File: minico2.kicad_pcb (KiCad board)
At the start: 2 copper layers, 40 parts, among them J1 USB_C_Receptacle_USB2.0, J2 GDEY0213Z98, Q1 MMBT2222, Q2 MMBT2222, Q3 Q_NMOS_GSD, U1 ESP32-WROOM-32E, U2 CH340C, U3 TLV62568DBV, U4 SHT31-DIS, U5 SCD30

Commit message: Route PCB
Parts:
- removed C3: 6.8pF, Capacitor_SMD:C_0402_1005Metric
- removed C5: 100nF, Capacitor_SMD:C_0402_1005Metric
- removed R7, R8: 10kΩ, Resistor_SMD:R_0402_1005Metric
- removed U4: SHT31-DIS, Sensor_Humidity:Sensirion_DFN-8-1EP_2.5x2.5mm_P0.5mm_EP1.1x1.7mm
- added H1: MountingHole, MountingHole:MountingHole_2.7mm_M2.5, F.Cu at (129.0, 79.0)
- added H2: MountingHole, MountingHole:MountingHole_2.7mm_M2.5, F.Cu at (176.0, 79.0)
- added H3: MountingHole, MountingHole:MountingHole_2.7mm_M2.5, F.Cu at (129.0, 126.0)
- added H4: MountingHole, MountingHole:MountingHole_2.7mm_M2.5, F.Cu at (176.0, 126.0)
- added TP1: TestPoint_Small, TestPoint:TestPoint_Pad_D2.0mm, F.Cu at (130.9, 88.5)
- added TP2: TestPoint_Small, TestPoint:TestPoint_Pad_D2.0mm, F.Cu at (130.9, 91.5)
- added TP3: TestPoint_Small, TestPoint:TestPoint_Pad_D2.0mm, F.Cu at (130.9, 85.4)
- added TP4: TestPoint_Small, TestPoint:TestPoint_Pad_D1.0mm, F.Cu at (139.4, 97.2)
- added TP5: TestPoint_Small, TestPoint:TestPoint_Pad_D1.0mm, F.Cu at (137.0, 94.3)
- added TP6: TestPoint_Small, TestPoint:TestPoint_Pad_D1.0mm, F.Cu at (142.8, 102.5)
- added TP7: TestPoint_Small, TestPoint:TestPoint_Pad_D1.0mm, F.Cu at (138.7, 102.6)
- C1: value 10nF -> 100nF; footprint Capacitor_SMD:C_0402_1005Metric -> Capacitor_SMD:C_0603_1608Metric
- C10, C11, C12, C13, C14, C15, C2, C4, C7, C8: footprint Capacitor_SMD:C_0402_1005Metric -> Capacitor_SMD:C_0603_1608Metric
- C9: value 1µF 25F -> 1µF 25V; footprint Capacitor_SMD:C_0402_1005Metric -> Capacitor_SMD:C_0603_1608Metric
- L2: footprint Inductor_SMD:L_1008_2520Metric -> Inductor_SMD:L_Taiyo-Yuden_NR-60xx
- Q3: value Q_NMOS_GSD -> IRLML0100TRPBF
- R1, R10, R2, R4, R5, R6, R9: footprint Resistor_SMD:R_0402_1005Metric -> Resistor_SMD:R_0603_1608Metric
- R3: value 450kΩ -> 453kΩ; footprint Resistor_SMD:R_0402_1005Metric -> Resistor_SMD:R_0603_1608Metric
- U3: value TLV62568DBV -> AP3418; footprint Package_TO_SOT_SMD:SOT-23-5 -> minico2:SOT-25
- moved J2 146.4 mm to (174.2, 96.2), turned to 90 degrees
- moved R9 144.7 mm to (168.8, 93.7), turned to -90 degrees
- moved D2 144.3 mm to (174.9, 83.2), turned to 180 degrees
- moved D3 135.3 mm to (166.8, 90.6), turned to 90 degrees
- moved R10 131.8 mm to (170.4, 93.7), turned to -90 degrees
- moved C11 127.4 mm to (170.9, 98.0), turned to 180 degrees
- moved R3 120.4 mm to (138.6, 87.2), turned to -90 degrees
- moved L2 120.3 mm to (167.5, 84.9)
- moved R6 113.8 mm to (137.3, 98.8), turned to 90 degrees
- moved R5 113.2 mm to (127.8, 98.8), turned to 90 degrees
- moved U5 109.9 mm to (155.0, 117.0), turned to 90 degrees
- moved C7 103.8 mm to (171.8, 83.9), turned to -90 degrees
- moved C2 99.6 mm to (135.8, 91.0)
- moved C10 96.7 mm to (172.0, 93.7), turned to -90 degrees
- moved U1 95.7 mm to (151.8, 91.0)
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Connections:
- net /SCL renamed /SCD30_SCL
- net /SDA renamed /SCD30_SDA
- net /VCOM renamed Net-(C15-Pad1)
- net Net-(J1-PadA6) renamed /D+
- net Net-(J1-PadA7) renamed /D-
- J2 pad 10: unconnected-(J2-Pad10) -> /~{RES}
- J2 pad 11: unconnected-(J2-Pad11) -> /D/C
- J2 pad 12: unconnected-(J2-Pad12) -> /~{CS}
- J2 pad 13: unconnected-(J2-Pad13) -> /DISPLAY_SCL
- J2 pad 14: unconnected-(J2-Pad14) -> /DISPLAY_SDA
- J2 pad 9: unconnected-(J2-Pad9) -> /BUSY
- U1 pad 26: unconnected-(U1-Pad26) -> /DISPLAY_SDA
- U1 pad 27: unconnected-(U1-Pad27) -> /DISPLAY_SCL
- U1 pad 28: unconnected-(U1-Pad28) -> /~{CS}
- U1 pad 29: unconnected-(U1-Pad29) -> /D/C
- U1 pad 30: unconnected-(U1-Pad30) -> /~{RES}
- U1 pad 31: unconnected-(U1-Pad31) -> /BUSY
- U1 pad 6: /S8_RX -> unconnected-(U1-Pad6)
- U1 pad 7: /S8_TX -> unconnected-(U1-Pad7)
- U2 pad 16: +3V3 -> +5V
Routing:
- net +3V3: track 0.00 -> 123.0 mm, vias 0 -> 4
- net +5V: track 0.00 -> 53.8 mm, vias 0 -> 4
- net /ESP_RX: track 0.00 -> 44.4 mm, vias 0 -> 3
- net /ESP_TX: track 0.00 -> 42.9 mm, vias 0 -> 3
- net /SCD30_SDA: track 0.00 -> 41.0 mm, vias 0 -> 1
- net /SCD30_SCL: track 0.00 -> 36.5 mm
- net /GPIO0: track 0.00 -> 29.5 mm, vias 0 -> 3
- net /D+: track 0.00 -> 28.1 mm
- net /D/C: track 0.00 -> 26.5 mm, vias 0 -> 2
- net /DISPLAY_SCL: track 0.00 -> 26.2 mm, vias 0 -> 2
- net /~{CS}: track 0.00 -> 26.0 mm, vias 0 -> 2
- net /EN: track 0.00 -> 25.9 mm, vias 0 -> 3
- net /D-: track 0.00 -> 25.9 mm
- net /DISPLAY_SDA: track 0.00 -> 25.5 mm, vias 0 -> 2
- net GND: track 0.00 -> 24.9 mm, vias 0 -> 27
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- added copper zone on B.Cu, net GND
- added copper zone on F.Cu, net GND
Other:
- board outline added: 55 x 55 mm

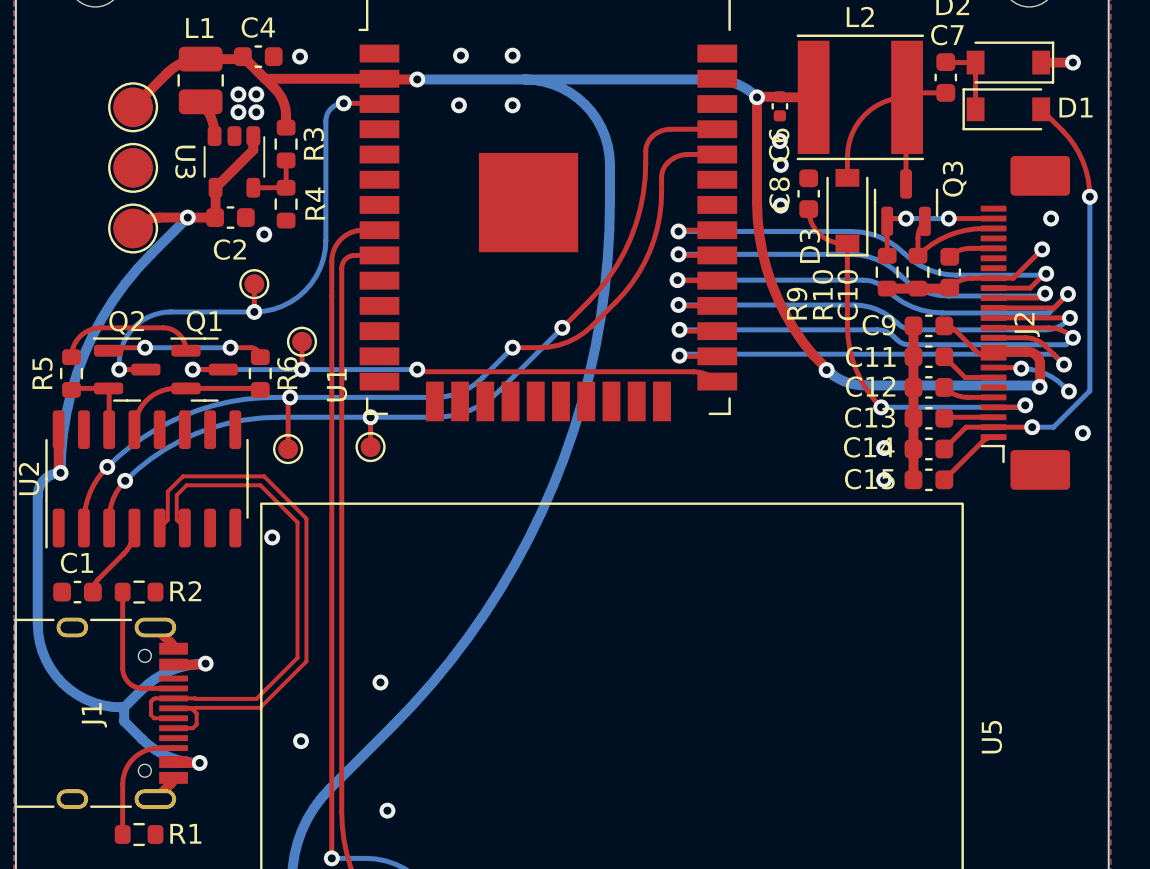
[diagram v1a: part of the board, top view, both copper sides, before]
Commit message: Fillet some tracks to prepare for production
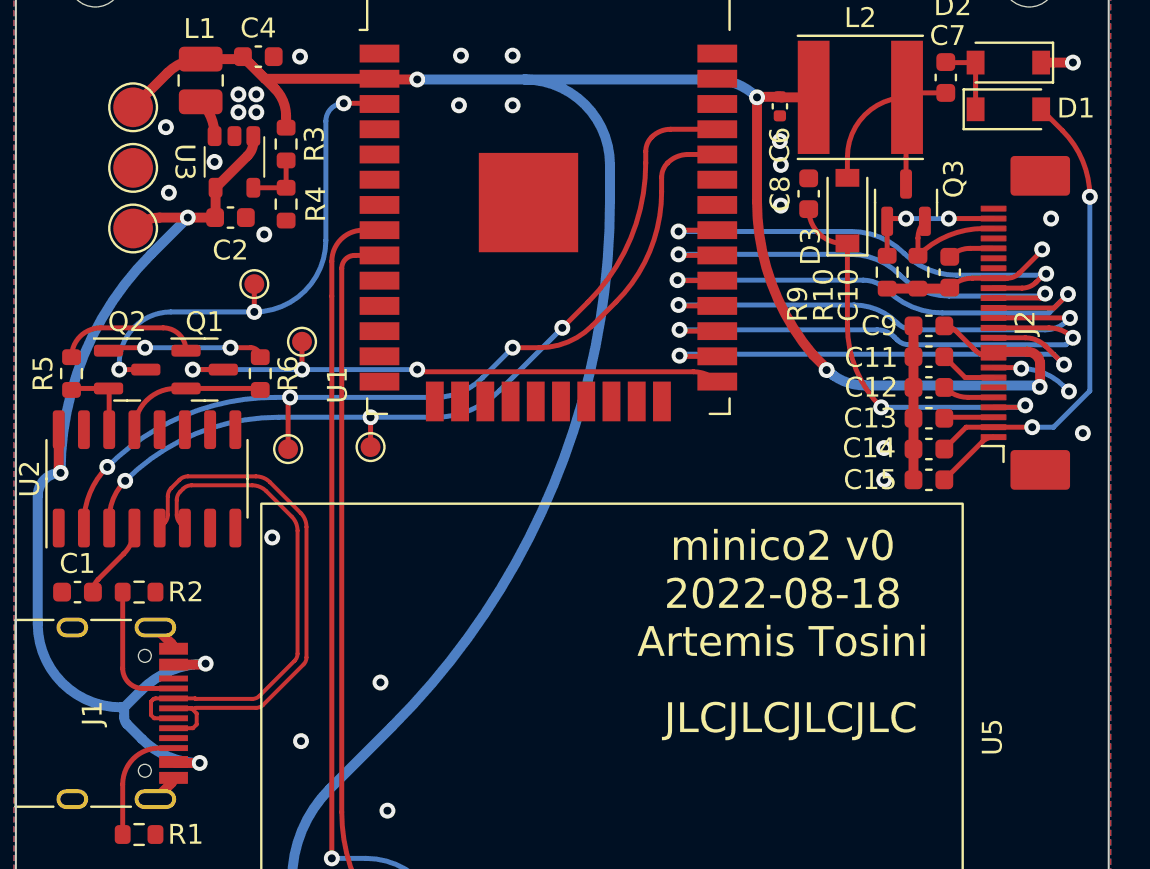
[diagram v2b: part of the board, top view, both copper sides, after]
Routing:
- net GND: vias 27 -> 30
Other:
- board text added: "JLCJLCJLCJLC"
- board text added: "minico2 v0 2022-08-18 Artemis Tosini"

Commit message: Ready for 1st production run
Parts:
- C6: footprint Capacitor_SMD:C_0402_1005Metric -> Capacitor_SMD:C_0603_1608Metric
- moved U5 7.44 mm to (159.4, 123.0)
- moved H4 7.07 mm to (181.0, 131.0)
- moved H2 5.00 mm to (181.0, 79.0)
- moved H3 5.00 mm to (129.0, 131.0)
- moved C6 0.38 mm to (163.3, 85.7)
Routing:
- net /SCD30_SDA: track 41.0 -> 48.9 mm
- net +3V3: track 123.0 -> 130.7 mm
- net /SCD30_SCL: track 36.5 -> 44.1 mm
- net /VGL: track 23.5 -> 26.1 mm, vias 2 -> 0
- net /D-: track 25.6 -> 27.8 mm
- net GND: track 24.9 -> 26.9 mm, vias 30 -> 35
- net /~{CS}: track 26.0 -> 27.7 mm
- net /~{RES}: track 23.7 -> 24.9 mm
- net /DISPLAY_SCL: track 26.2 -> 27.4 mm
- net /D/C: track 26.5 -> 27.3 mm
- net /BUSY: track 24.0 -> 23.2 mm
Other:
- board size 55 x 55 mm -> 60 x 60 mm
- board text added: "minico2 v0 2022-08-18 artemist"
- board text removed: "minico2 v0 2022-08-18 Artemis Tosini"
